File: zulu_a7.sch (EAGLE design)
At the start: 183 parts, among them J1 Pmod 2x6, Q1 12MHz 25ppm (FPGA + FT2232HQ), Q2 2N7002, Q3 MBT3904DW1T1, U1 XC7A35T-1CPG236C, U10 93LC46BT-I/SN, U2 FT2232HQ USB-UART/JTAG Bridge, U3 AS4C32M16SB-6TIN, U4 W25Q128JVSIQ, U8 LTC3569EUDC#TRPBF, X1 Molex 105017-0001 Micro-USB-B, X2 ZULU-CONN, X3 MICROSD_CONDM3AT-SF-PEJM5

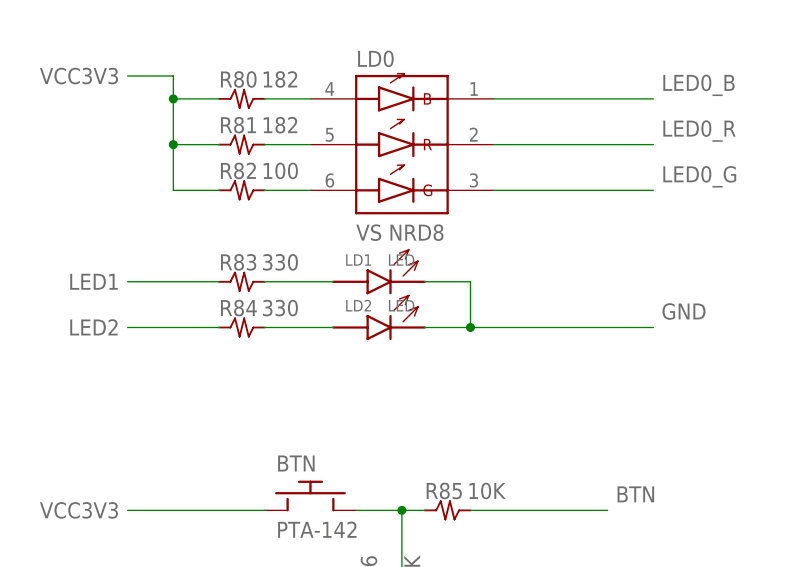
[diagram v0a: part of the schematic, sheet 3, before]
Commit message: LD1, LD2 and R34 get part numbers; no unidentifiable part left
R34 is the microSD DAT0-3 pull-ups and ALL FOUR elements are used -- which is
what an array is for, and why this one stays an array where R1, R2 and R4 used
2, 3 and 6 of theirs and were better off split. 4.7k was already the value; only
the number was missing. CTS 742C083472JTR, and 5 percent where the discretes on
this board are 1, because a pull-up does not care.

LD1 and LD2 are user status LEDs off FPGA pins through R83/R84 at 330R, so
(3.3 - Vf)/330: 3.9 mA green, 4.2 red, 3.6 yellow, 1.2 blue. Any of the first
three is comfortable and well inside an LVCMOS33 pin's 12 mA. They are twice as
bright as LD5's 1.9 mA, which is right for something a user watches rather than
a rail indicator.

RED IS A PREFERENCE AND THE NOTE SAYS SO. The circuit takes green just as
happily. Red so the two user LEDs read differently from LD5, which is green and
means power good -- on a board being brought up, telling those apart at a glance
is worth something. Same LTST-C191 family and 0603 land as LD5, so one catalogue
line rather than two.

Lines with no MANF# fall 16 to 14, and none of the 14 is a hole any more: 13
carry the part number in the value field (AS4C32M16SB-6TIN, LTC3569EUDC#TRPBF,
XC7A35T-1CPG236C and so on) and the fourteenth is X2, which is the board's own
pin field and not a thing you buy. Moving those into MANF# is tidying, not a gap.

Co-Authored-By: Claude Opus 5 <noreply@anthropic.com>
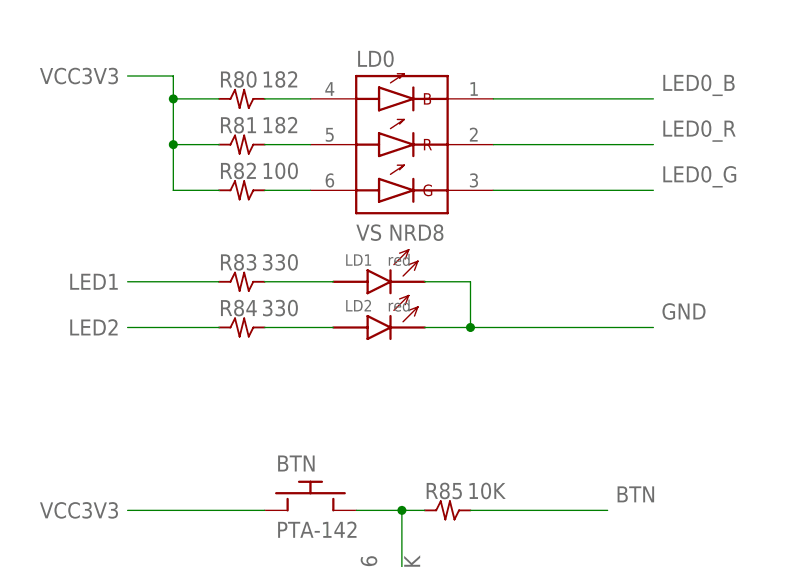
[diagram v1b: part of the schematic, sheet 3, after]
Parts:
- LD1, LD2: value LED -> red; MANF (none) -> Lite-On; MANF# (none) -> LTST-C191KRKT; NOTE (none) -> User status LED, driven straight off an FPGA pin through R8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; SPEC (none) -> red indicator, 0603, Vf 2.1V max at 4mA
- R34: MANF (none) -> CTS; MANF# (none) -> 742C083472JTR; NOTE (none) -> The microSD DAT0-3 pull-ups, all four elements used -- whic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; SPEC (none) -> 4-element isolated resistor array, 4.7k, 5 percent or bette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
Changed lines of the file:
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@@
 <attribute name="MANF#" value="DM3AT-SF-PEJM5"/>
 </part>
-<part name="R34" library="ctambe" deviceset="RES4" device="742" value="4.7K"/>
+<part name="R34" library="ctambe" deviceset="RES4" device="742" value="4.7K">
+<attribute name="MANF" value="CTS"/>
+<attribute name="MANF#" value="742C083472JTR"/>
+<attribute name="SPEC" value="4-element isolated resistor array, 4.7k, 5 percent or better, 742C083 8-pin convex land"/>
+<attribute name="NOTE" value="The microSD DAT0-3 pull-ups, all four elements used -- which is what an array is actually for, unlike R1, R2 and R4, which used 2, 3 and 6 of theirs and were split into discretes. This one stays an array. 4.7k is the conventional value for SD data lines and it was already chosen; only the part number was missing. 5 percent is ample for a pull-up, so this is a J part where the discrete resistors on this board are F. CTS 742C is the family the footprint is named after. Confirm the suffix -- it encodes tolerance and packaging and is the easy thing to get wrong."/>
+</part>
 <part name="R35" library="rcl" deviceset="R-US_" device="R0402" value="4.7K">
 <attribute name="MANF" value="Yageo"/>
@@
 </part>
 <part name="LD0" library="ctambe" deviceset="LED_RGB" device="" value="VS NRD8"/>
-<part name="LD1" library="ctambe" deviceset="LED" device="" value="LED"/>
-<part name="LD2" library="ctambe" deviceset="LED" device="" value="LED"/>
+<part name="LD1" library="ctambe" deviceset="LED" device="" value="red">
+<attribute name="MANF" value="Lite-On"/>
+<attribute name="MANF#" value="LTST-C191KRKT"/>
+<attribute name="SPEC" value="red indicator, 0603, Vf 2.1V max at 4mA"/>
+<attribute name="NOTE" value="User status LED, driven straight off an FPGA pin through R83 at 330R: (3.3 - Vf)/330 is 3.9 mA green, 4.2 red, 3.6 yellow, and 1.2 mA blue or white. Any of the first three is comfortable and well inside an LVCMOS33 pin's 12 mA. RED IS A PREFERENCE, NOT A CONSTRAINT -- the circuit takes green just as happily. It is red so that the two user LEDs read differently from LD5, which is green and means power good; on a board being brought up that is worth being able to tell apart at a glance. Same LTST-C191 family and the same 0603 land as LD5, so it is one line in the catalogue, not two. Confirm the suffix before ordering."/>
+</part>
+<part name="LD2" library="ctambe" deviceset="LED" device="" value="red">
+<attribute name="MANF" value="Lite-On"/>
+<attribute name="MANF#" value="LTST-C191KRKT"/>
+<attribute name="SPEC" value="red indicator, 0603, Vf 2.1V max at 4mA"/>
+<attribute name="NOTE" value="User status LED, driven straight off an FPGA pin through R84 at 330R: (3.3 - Vf)/330 is 3.9 mA green, 4.2 red, 3.6 yellow, and 1.2 mA blue or white. Any of the first three is comfortable and well inside an LVCMOS33 pin's 12 mA. RED IS A PREFERENCE, NOT A CONSTRAINT -- the circuit takes green just as happily. It is red so that the two user LEDs read differently from LD5, which is green and means power good; on a board being brought up that is worth being able to tell apart at a glance. Same LTST-C191 family and the same 0603 land as LD5, so it is one line in the catalogue, not two. Confirm the suffix before ordering."/>
+</part>
 <part name="BTN" library="ctambe" deviceset="SWITCH_TACT" device="" value="PTA-142"/>
 <part name="Q1" library="ctambe" deviceset="OSC_CHIP" device="ASEM1-12MHZ" value="12MHz 25ppm (FPGA + FT2232HQ)"/>

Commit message: Move ten real part numbers out of Value and into MANF#
U1, U3, U8, U10, D1, D2, D3, Q3, X1, U2. Value keeps them too -- a person
reading the schematic wants to see XC7A35T-1CPG236C on the symbol -- but MANF#
is what a purchasing system reads, and it was empty on all ten.

Two were not a straight copy. X1's value is "Molex 105017-0001 Micro-USB-B", a
description with the number inside it, so MANF# takes 105017-0001 and Molex goes
to MANF. And U2's value names the chip, not the part: FT2232HQ is the device,
FT2232HQ-REEL is what you order. Q3 gained its G suffix for the same reason --
MBT3904DW1T1G is the orderable lead-free part.

FOUR ARE STILL EMPTY AND NONE OF THEM IS A MOVE, WHICH IS WHY THEY ARE STILL
EMPTY. "Pmod 2x6" and "12MHz 25ppm (FPGA + FT2232HQ)" are descriptions, not
numbers -- J1 needs a real 2x6 0.1 in socket chosen and Q1 a real 12 MHz
oscillator in the 3.2 x 2.5 package. "PTA-142" and "VS NRD8" are series
designations; the library knows Victory makes the NRD8 but neither carries a
full orderable number, and I am not going to invent one. X2 has no value at all
and needs none: it is the board's own pin field, not a thing you buy.

Found while reading those: SWITCH_TACT and LED_RGB both still said "NO PACKAGE
ASSIGNED -- the land pattern must be added before layout". Both packages have
been assigned and drawn from their datasheets for some time; the warning was
left behind when they were. A note telling you to do something already done is
worse than no note, so both now say what is actually true.

Co-Authored-By: Claude Opus 5 <noreply@anthropic.com>
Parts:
- D1, D2: MANF (none) -> Nexperia; MANF# (none) -> PMEG2020EJ,115
- D3: MANF (none) -> Littelfuse; MANF# (none) -> SMF5.0A
- Q3: MANF (none) -> onsemi; MANF# (none) -> MBT3904DW1T1G
- U1: MANF# (none) -> XC7A35T-1CPG236C
- U10: MANF# (none) -> 93LC46BT-I/SN
- U2: MANF (none) -> FTDI; MANF# (none) -> FT2232HQ-REEL
- U3: MANF (none) -> Alliance Memory; MANF# (none) -> AS4C32M16SB-6TIN
- U8: MANF (none) -> Analog Devices; MANF# (none) -> LTC3569EUDC#TRPBF
- X1: MANF (none) -> Molex; MANF# (none) -> 105017-0001
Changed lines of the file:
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@@
 <part name="U3" library="ctambe" deviceset="SDRAM-X16" device="-ALLIANCE-512M" value="AS4C32M16SB-6TIN">
 <attribute name="NOTE" value="512Mbit (32M x 16) = 64MB. Pin-for-pin and dimensionally identical to the 256Mb AS4C16M16SA-6TIN it replaces: all 54 pins and every TSOP-II dimension were checked against both datasheets, and pin 40 is NC on both. ONE DIFFERENCE, AND IT IS NOT A PIN -- the column address is A0-A9 (1024 columns) instead of A0-A8 (512). The memory controller must be set to 10 column bits or it reaches only half the array. Row A0-A12, banks BA0/BA1 and refresh (8192 cycles/64ms) are unchanged. IDD1 rises 60mA to 120mA on the 600mA VCC3V3 buck (LTC3569 SW3)."/>
+<attribute name="MANF" value="Alliance Memory"/>
+<attribute name="MANF#" value="AS4C32M16SB-6TIN"/>
 </part>
 <part name="U4" library="ctambe" deviceset="SPI_FLASH" device="-SOIC_150_208" value="W25Q128JVSIQ">
@@
 <part name="U1" library="ctambe" deviceset="XC7A35T-CPG236" device="-1CPG236C" value="XC7A35T-1CPG236C">
 <attribute name="MANF" value="AMD/Xilinx"/>
+<attribute name="MANF#" value="XC7A35T-1CPG236C"/>
 </part>
 <part name="R10" library="rcl" deviceset="R-US_" device="R0201" value="2.32K">
@@
 <attribute name="SPEC" value="X7R 50V +-10%, 0.50 mm max"/>
 </part>
-<part name="U2" library="ctambe" deviceset="FT2232HQ" device="-QFN64" value="FT2232HQ USB-UART/JTAG Bridge"/>
+<part name="U2" library="ctambe" deviceset="FT2232HQ" device="-QFN64" value="FT2232HQ USB-UART/JTAG Bridge">
+<attribute name="MANF" value="FTDI"/>
+<attribute name="MANF#" value="FT2232HQ-REEL"/>
+</part>
 <part name="U10" library="ctambe" deviceset="EEPROM-93LC46B" device="-I/SN" value="93LC46BT-I/SN">
 <attribute name="MANF" value="Microchip"/>
+<attribute name="MANF#" value="93LC46BT-I/SN"/>
 </part>
 <part name="JP3" library="pinhead" deviceset="TESTPT-1X3" device="NOSILK" value="JTAG TCK/TMS/GND">
@@
 </part>
 <part name="GND1" library="ctambe" deviceset="GND" device=""/>
-<part name="U8" library="ctambe" deviceset="LTC3569" device="-UDC" value="LTC3569EUDC#TRPBF"/>
-<part name="D1" library="ctambe" deviceset="DIODE" device="" value="PMEG2020EJ,115"/>
-<part name="D2" library="ctambe" deviceset="DIODE" device="" value="PMEG2020EJ,115"/>
-<part name="D3" library="ctambe" deviceset="TVS" device="" value="SMF5.0A"/>
+<part name="U8" library="ctambe" deviceset="LTC3569" device="-UDC" value="LTC3569EUDC#TRPBF">
+<attribute name="MANF" value="Analog Devices"/>
+<attribute name="MANF#" value="LTC3569EUDC#TRPBF"/>
+</part>
+<part name="D1" library="ctambe" deviceset="DIODE" device="" value="PMEG2020EJ,115">
+<attribute name="MANF" value="Nexperia"/>
+<attribute name="MANF#" value="PMEG2020EJ,115"/>
+</part>
+<part name="D2" library="ctambe" deviceset="DIODE" device="" value="PMEG2020EJ,115">
+<attribute name="MANF" value="Nexperia"/>
+<attribute name="MANF#" value="PMEG2020EJ,115"/>
+</part>
+<part name="D3" library="ctambe" deviceset="TVS" device="" value="SMF5.0A">
+<attribute name="MANF" value="Littelfuse"/>
+<attribute name="MANF#" value="SMF5.0A"/>
+</part>
 <part name="GND24" library="ctambe" deviceset="GND" device=""/>
 <part name="C78" library="rcl" deviceset="C-GENERIC" device="C0805" value="22uF 10V">
@@
 <attribute name="SPEC" value="X5R 6.3V +-20%, 0.90 mm max"/>
 </part>
-<part name="Q3" library="ctambe" deviceset="NPN-DUAL" device="" value="MBT3904DW1T1"/>
+<part name="Q3" library="ctambe" deviceset="NPN-DUAL" device="" value="MBT3904DW1T1">
+<attribute name="MANF" value="onsemi"/>
+<attribute name="MANF#" value="MBT3904DW1T1G"/>
+</part>
 <part name="R75" library="rcl" deviceset="R-US_SMALL" device="R0402" value="100K">
 <attribute name="MANF" value="Yageo"/>
@@
 </part>
 <part name="GND8" library="ctambe" deviceset="GND" device=""/>
-<part name="X1" library="ctambe" deviceset="MINI-USB-" device="105017-0001" value="Molex 105017-0001 Micro-USB-B"/>
+<part name="X1" library="ctambe" deviceset="MINI-USB-" device="105017-0001" value="Molex 105017-0001 Micro-USB-B">
+<attribute name="MANF" value="Molex"/>
+<attribute name="MANF#" value="105017-0001"/>
+</part>
 <part name="GND4" library="ctambe" deviceset="GND" device=""/>
 <part name="GND3" library="ctambe" deviceset="GND" device=""/>

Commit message: J1 and Q1 get real parts; only the two datasheet-bound ones are left
Q1 -> Abracon ASEM1-12.000MHZ-LC-T. THE SCHEMATIC SAYS IT IS AN OSCILLATOR AND
NOT A CRYSTAL: pin 2 to GND, pin 4 to VCC3V3, pin 3 out into R24 and R25, pin 1
tied high. A crystal would be two pads and a pair of load capacitors. The
frequency was never a choice either -- the FT2232H wants 12 MHz for its USB PLL,
so it was fixed before the rest of the board existed. 25 ppm is the figure
already in the value and is inside what FTDI asks of the reference. Pin 1 to Vdd
suits an OE part or one with pin 1 unconnected, so that does not narrow it. The
design note had already named the ASEM1 family for the oscillator it replaced.

J1 -> Sullins PPTC062LFBN-RC, A SOCKET, AND THE LIBRARY NAME ARGUES OTHERWISE.
The package is called "PIN HEADER 2x6" and the deviceset PINHD-2X6, which is
inherited naming. On a Digilent Pmod the HOST carries the female socket and the
module carries the pins -- Cmod A7 included. Order male pins off that library
name and no Pmod will mate. The footprint is twelve plated holes on 2.54 either
way, so PRPC006DAAN-RC drops into the same land if pins and a cable are wanted
instead; the note on the part says so. 8.5 mm of height is fine because J1 is on
the FRONT, and it is the back that faces the breadboard.

Lines with no MANF# are down to three, and none is a move I can make: BTN's
"PTA-142" and LD0's "VS NRD8" are series names whose full ordering numbers are
in datasheets I do not have -- the library knows Victory makes the NRD8 and that
both land patterns were drawn from real drawings, so those drawings are where
the numbers are. X2 is the board's own pin field and is not bought.

Co-Authored-By: Claude Opus 5 <noreply@anthropic.com>
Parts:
- J1: MANF (none) -> Sullins; MANF# (none) -> PPTC062LFBN-RC; NOTE (none) -> A SOCKET, NOT PINS, AND THE LIBRARY NAME DISAGREES WITH THA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; SPEC (none) -> 2x6 female header, 2.54 mm pitch, through-hole, 12 way -- P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
- Q1: MANF (none) -> Abracon; MANF# (none) -> ASEM1-12.000MHZ-LC-T; NOTE (none) -> ACTIVE OSCILLATOR, NOT A CRYSTAL -- the schematic settles i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; SPEC (none) -> 12.000 MHz CMOS oscillator, 3.3V, 25 ppm, 3.2 x 2.5 mm 4-pa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
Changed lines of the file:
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@@
 </part>
 <part name="BTN" library="ctambe" deviceset="SWITCH_TACT" device="" value="PTA-142"/>
-<part name="Q1" library="ctambe" deviceset="OSC_CHIP" device="ASEM1-12MHZ" value="12MHz 25ppm (FPGA + FT2232HQ)"/>
+<part name="Q1" library="ctambe" deviceset="OSC_CHIP" device="ASEM1-12MHZ" value="12MHz 25ppm (FPGA + FT2232HQ)">
+<attribute name="MANF" value="Abracon"/>
+<attribute name="MANF#" value="ASEM1-12.000MHZ-LC-T"/>
+<attribute name="SPEC" value="12.000 MHz CMOS oscillator, 3.3V, 25 ppm, 3.2 x 2.5 mm 4-pad, pin 1 enable or NC, pin 3 output"/>
+<attribute name="NOTE" value="ACTIVE OSCILLATOR, NOT A CRYSTAL -- the schematic settles it: pin 2 to GND, pin 4 to VCC3V3, pin 3 out into R24 and R25, and pin 1 tied to VCC3V3, which is a 4-pad XO with its enable held high. A crystal would have two pads and load capacitors. THE FREQUENCY IS NOT A CHOICE: the FT2232H wants 12 MHz for its USB PLL, so that was fixed before anything else. 25 ppm is the value already recorded and is comfortably inside what FTDI asks of the reference. Output drives two loads through 33R each, the FT2232's OSCI and the FPGA clock ball. Pin 1 to Vdd suits either an OE part or one with pin 1 not connected, so the choice is not narrowed by it. ASEM1 is the family the design note already named. Confirm the suffix -- it encodes stability and temperature range and is the easy thing to get wrong."/>
+</part>
 <part name="C38" library="rcl" deviceset="C-GENERIC" device="C0201" value="0.01uF">
 <attribute name="MANF" value="Murata"/>
@@
 <part name="SUPPLY12" library="ctambe" deviceset="VCC3V3" device=""/>
 <part name="SUPPLY13" library="ctambe" deviceset="VCC3V3" device=""/>
-<part name="J1" library="ctambe" deviceset="PINHD-2X6" device="" value="Pmod 2x6"/>
+<part name="J1" library="ctambe" deviceset="PINHD-2X6" device="" value="Pmod 2x6">
+<attribute name="MANF" value="Sullins"/>
+<attribute name="MANF#" value="PPTC062LFBN-RC"/>
+<attribute name="SPEC" value="2x6 female header, 2.54 mm pitch, through-hole, 12 way -- Pmod host socket"/>
+<attribute name="NOTE" value="A SOCKET, NOT PINS, AND THE LIBRARY NAME DISAGREES WITH THAT. The package is called PIN HEADER 2x6 and the deviceset PINHD-2X6, which is inherited naming, but on a Digilent Pmod the HOST carries the female socket and the peripheral module carries the male pins that plug into it. Cmod A7 is the same. Order male pins off that library name and no Pmod will mate. The footprint is 12 plated holes on 2.54 either way, so a male header such as Sullins PRPC006DAAN-RC drops into the same land if you would rather have pins and a cable. Height 8.5 mm is not a problem: J1 is on the FRONT, and it is the back that faces a breadboard a couple of millimetres away."/>
+</part>
 <part name="R24" library="rcl" deviceset="R-US_SMALL" device="R0201" value="33">
 <attribute name="MANF" value="Yageo"/>
